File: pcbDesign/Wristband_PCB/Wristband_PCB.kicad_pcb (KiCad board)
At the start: 2 copper layers, 46.2 x 44 mm, 4 parts, among them U1 module_adxl345, U2 SEN0344, U3 ESP32-C3_SUPERMINI_TH

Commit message: gerber-flip
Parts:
- moved U1 32.4 mm to (119.3, 82.8), turned to 0 degrees
- moved U3 15.8 mm to (142.3, 75.6), turned to 180 degrees
- moved U2 2.35 mm to (133.9, 75.9), turned to 0 degrees
- moved DS1 0.37 mm to (134.7, 75.7)
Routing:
- net GND: track 67.8 -> 0.00 mm
- net /SCL: track 64.9 -> 101.6 mm
- net /SDA: track 70.6 -> 55.5 mm
- net +3.3V: track 51.2 -> 54.0 mm
- added copper zone on F.Cu, net GND
- removed copper zone on F.Cu, net (none)
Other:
- board size 46.2 x 44 mm -> 40 x 40 mm

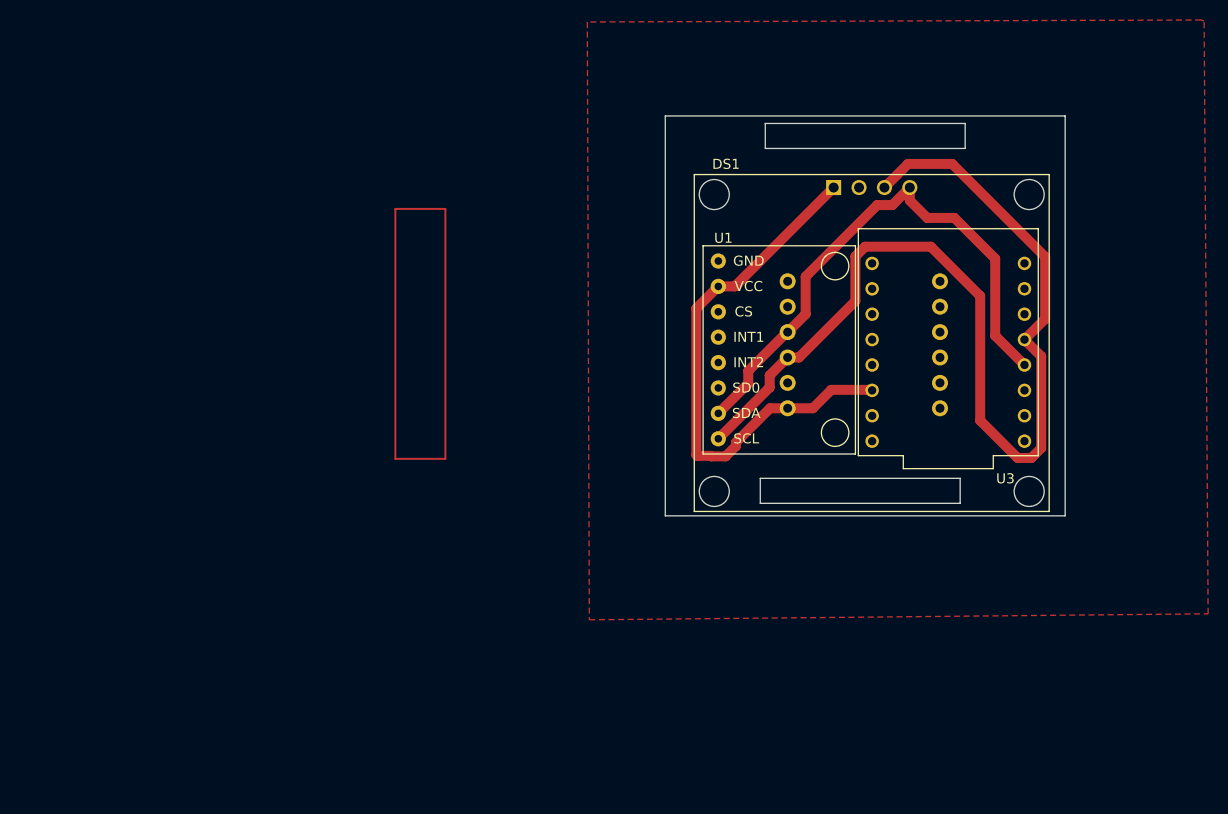
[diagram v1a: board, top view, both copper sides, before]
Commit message: buzzer added
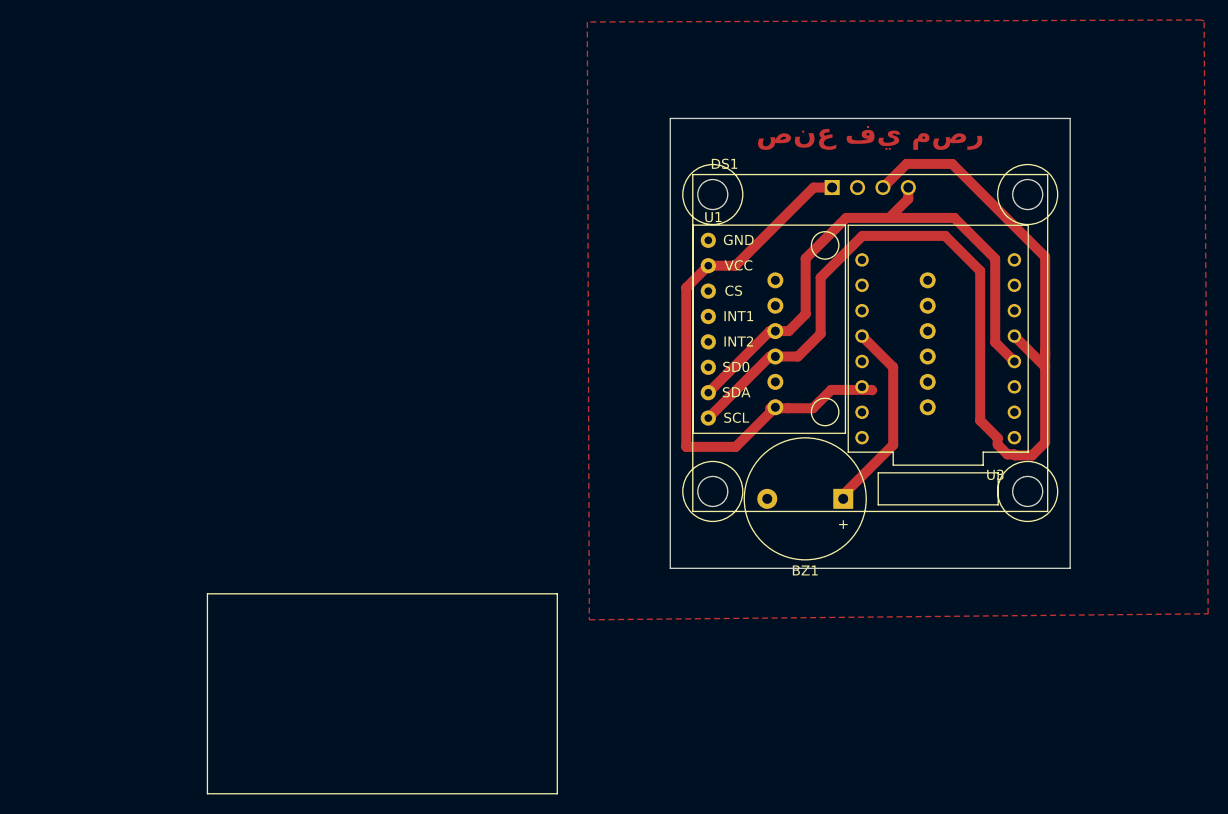
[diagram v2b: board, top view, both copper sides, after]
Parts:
- added BZ1: Buzzer, buzzer:Buzzer_12x9.5RM7.6, F.Cu at (131.8, 91.3)
- moved U1 2.30 mm to (118.3, 80.7)
- moved U2 1.23 mm to (132.6, 75.8)
- moved U3 1.07 mm to (141.3, 75.3)
- moved DS1 0.15 mm to (134.5, 75.7)
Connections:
- U3 pad 3: unconnected-(U3-GPIO3-Pad3) -> Net-(BZ1-+)
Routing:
- net Net-(BZ1-+): track 0.00 -> 19.8 mm
- net /SCL: track 101.6 -> 107.8 mm
- net +3.3V: track 54.0 -> 56.2 mm
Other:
- board size 40 x 40 mm -> 40 x 45 mm
- board text added: "صنع في مصر"

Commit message: added the power terminal and the resistor
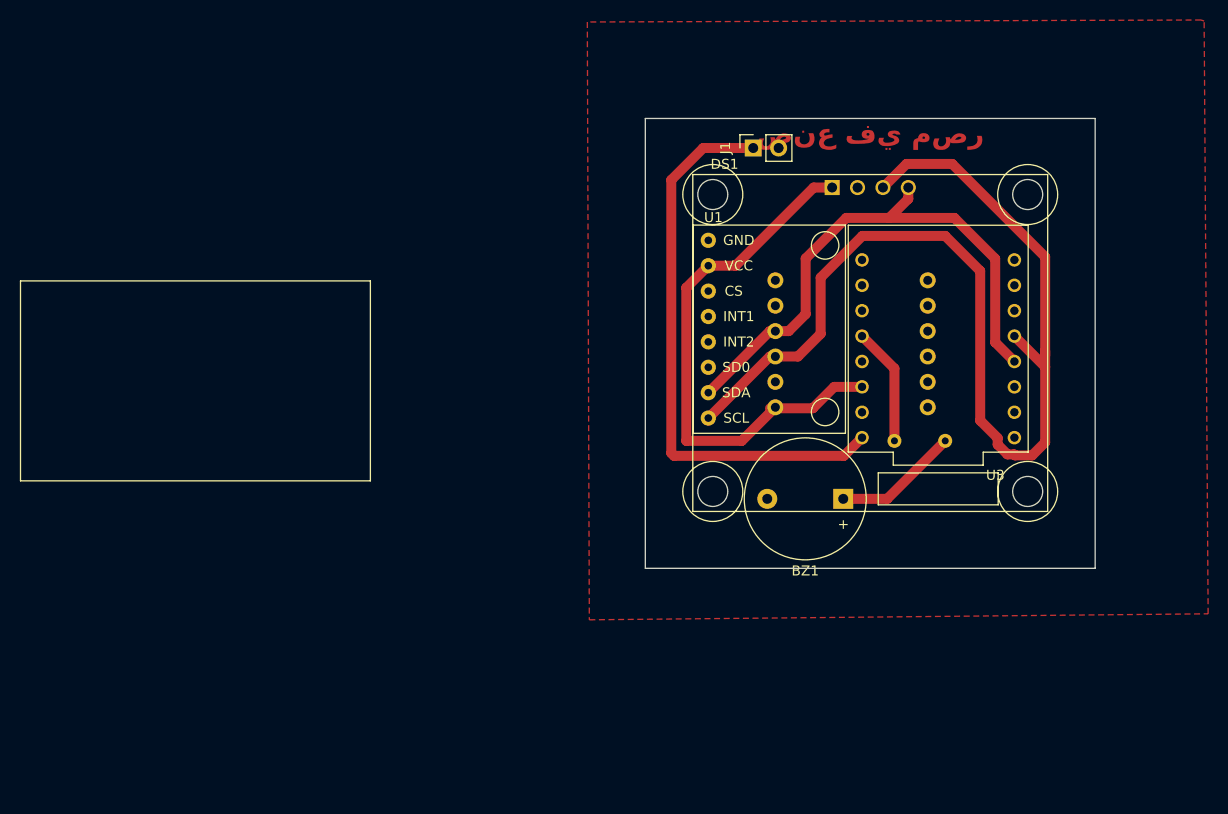
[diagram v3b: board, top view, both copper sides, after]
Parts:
- added J1: Conn_01x02_Socket, Connector_PinSocket_2.54mm:PinSocket_1x02_P2.54mm_Vertical, F.Cu at (122.8, 56.2)
- added R1: R, Resistor_THT:R_Axial_DIN0204_L3.6mm_D1.6mm_P5.08mm_Horizontal, B.Cu at (142.0, 85.5)
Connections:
- U3 pad 3: Net-(BZ1-+) -> Net-(U3-GPIO3)
- U3 pad 5V: unconnected-(U3-Pad5V) -> +5V
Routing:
- net +5V: track 0.00 -> 56.8 mm
- net Net-(U3-GPIO3): track 0.00 -> 11.8 mm
- net Net-(BZ1-+): track 19.8 -> 12.6 mm
- net +3.3V: track 56.2 -> 54.5 mm
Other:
- board size 40 x 45 mm -> 45 x 45 mm
